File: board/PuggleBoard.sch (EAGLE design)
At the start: 131 parts, among them U1 LMP7704, U10 SN65LVDS2, U11 SN65LVDS1, U12 SN65LVDS1, U13 SN65LVDS1, U14 SN65MLVD201D, U15 24C, U2 ADS8331, U3 OPA4209, U4 AD5686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

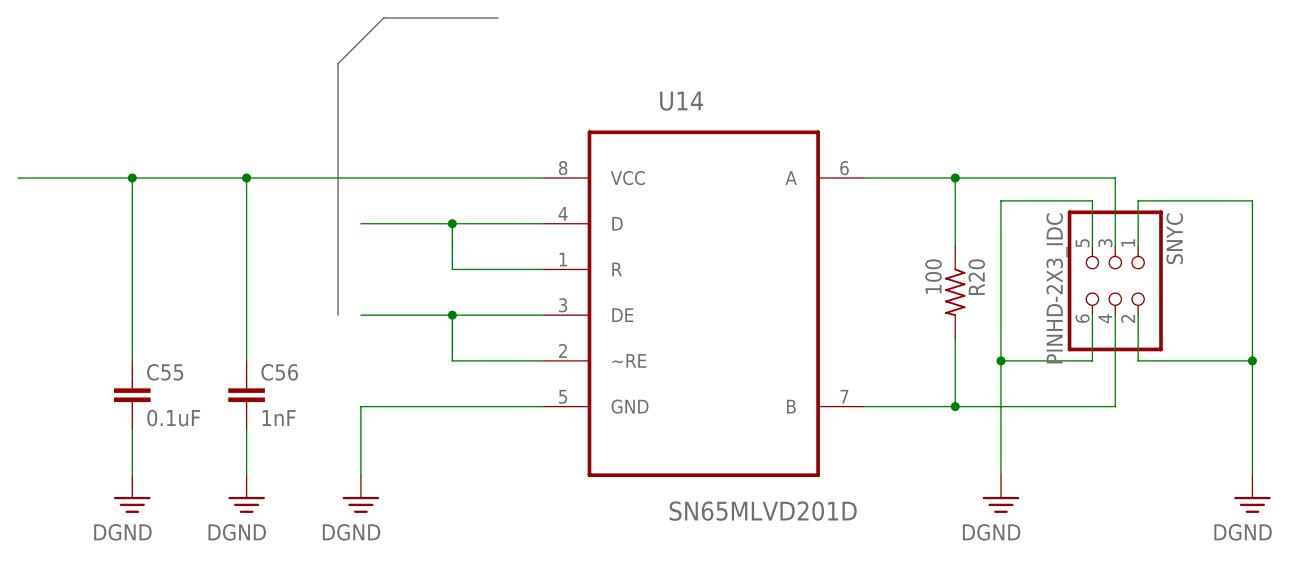
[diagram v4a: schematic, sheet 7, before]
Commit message: Did some of the differential pair wiring.
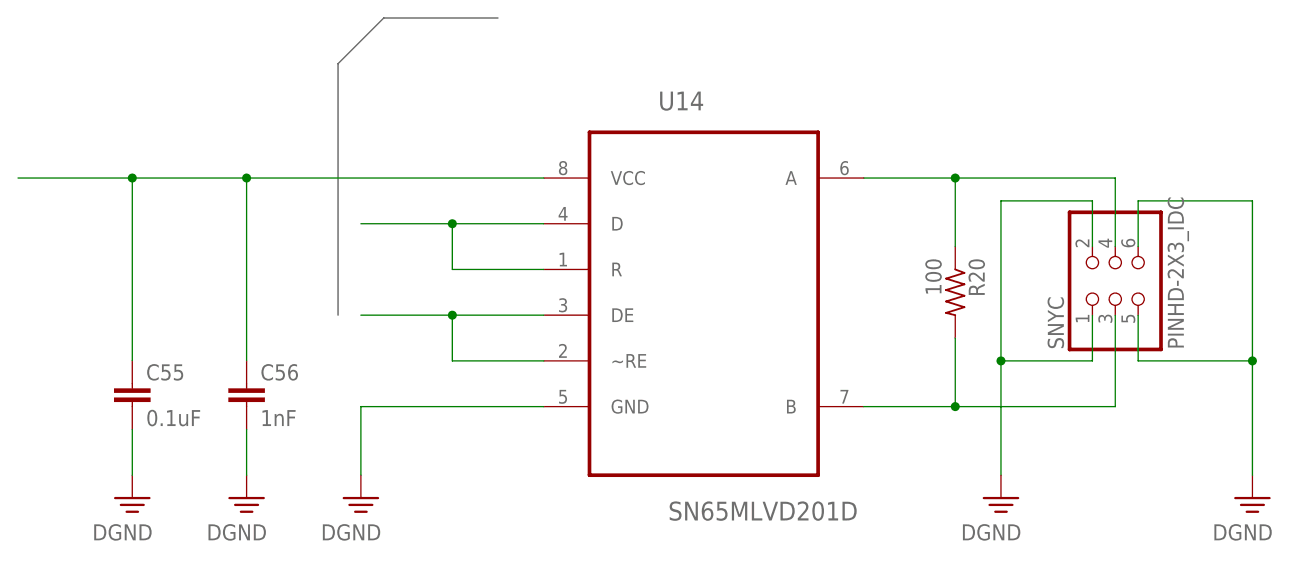
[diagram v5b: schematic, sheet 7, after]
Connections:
- removed net N$11: R20.2, SNYC.4, U14.B
- removed net N$7: R20.1, SNYC.3, U14.A
- new net SYNC_N: R20.2, SNYC.3, U14.B
- new net SYNC_P: R20.1, SNYC.4, U14.A
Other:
- moved on the sheet: SNYC
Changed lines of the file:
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@@
 <instance part="FRAME8" gate="G$2" x="172.72" y="0"/>
 <instance part="U14" gate="A" x="149.86" y="127"/>
-<instance part="SNYC" gate="G$1" x="195.58" y="121.92" rot="R270"/>
+<instance part="SNYC" gate="G$1" x="195.58" y="124.46" rot="R90"/>
 <instance part="R20" gate="R" x="177.8" y="121.92" rot="R270"/>
 <instance part="DGND12" gate="DGND" x="210.82" y="99.06"/>
@@
 </busses>
 <nets>
-<net name="N$11" class="0">
+<net name="SYNC_N" class="2">
 <segment>
 <pinref part="U14" gate="A" pin="B"/>
@@
 <pinref part="R20" gate="R" pin="2"/>
 <wire x1="177.8" y1="109.22" x2="177.8" y2="116.84" width="0.1524" layer="91"/>
-<pinref part="SNYC" gate="G$1" pin="4"/>
 <wire x1="177.8" y1="109.22" x2="195.58" y2="109.22" width="0.1524" layer="91"/>
+<junction x="177.8" y="109.22"/>
+<pinref part="SNYC" gate="G$1" pin="3"/>
 <wire x1="195.58" y1="109.22" x2="195.58" y2="119.38" width="0.1524" layer="91"/>
-<junction x="177.8" y="109.22"/>
 </segment>
 </net>
-<net name="N$7" class="0">
+<net name="SYNC_P" class="2">
 <segment>
 <pinref part="U14" gate="A" pin="A"/>
@@
 <pinref part="R20" gate="R" pin="1"/>
 <wire x1="177.8" y1="127" x2="177.8" y2="134.62" width="0.1524" layer="91"/>
-<pinref part="SNYC" gate="G$1" pin="3"/>
 <wire x1="177.8" y1="134.62" x2="195.58" y2="134.62" width="0.1524" layer="91"/>
+<junction x="177.8" y="134.62"/>
+<pinref part="SNYC" gate="G$1" pin="4"/>
 <wire x1="195.58" y1="134.62" x2="195.58" y2="127" width="0.1524" layer="91"/>
-<junction x="177.8" y="134.62"/>
 </segment>
 </net>
 <net name="GND" class="0">
 <segment>
-<pinref part="SNYC" gate="G$1" pin="1"/>
-<wire x1="198.12" y1="127" x2="198.12" y2="132.08" width="0.1524" layer="91"/>
 <wire x1="198.12" y1="132.08" x2="210.82" y2="132.08" width="0.1524" layer="91"/>
 <wire x1="210.82" y1="132.08" x2="210.82" y2="114.3" width="0.1524" layer="91"/>
-<pinref part="SNYC" gate="G$1" pin="2"/>
-<wire x1="198.12" y1="119.38" x2="198.12" y2="114.3" width="0.1524" layer="91"/>
 <wire x1="198.12" y1="114.3" x2="210.82" y2="114.3" width="0.1524" layer="91"/>
 <wire x1="210.82" y1="114.3" x2="210.82" y2="101.6" width="0.1524" layer="91"/>
 <junction x="210.82" y="114.3"/>
 <pinref part="DGND12" gate="DGND" pin="PE"/>
+<pinref part="SNYC" gate="G$1" pin="5"/>
+<wire x1="198.12" y1="114.3" x2="198.12" y2="119.38" width="0.1524" layer="91"/>
+<pinref part="SNYC" gate="G$1" pin="6"/>
+<wire x1="198.12" y1="132.08" x2="198.12" y2="127" width="0.1524" layer="91"/>
 </segment>
 <segment>
-<pinref part="SNYC" gate="G$1" pin="5"/>
-<wire x1="193.04" y1="127" x2="193.04" y2="132.08" width="0.1524" layer="91"/>
 <wire x1="193.04" y1="132.08" x2="182.88" y2="132.08" width="0.1524" layer="91"/>
 <wire x1="182.88" y1="132.08" x2="182.88" y2="114.3" width="0.1524" layer="91"/>
-<pinref part="SNYC" gate="G$1" pin="6"/>
 <wire x1="182.88" y1="114.3" x2="182.88" y2="101.6" width="0.1524" layer="91"/>
-<wire x1="193.04" y1="119.38" x2="193.04" y2="114.3" width="0.1524" layer="91"/>
 <wire x1="193.04" y1="114.3" x2="182.88" y2="114.3" width="0.1524" layer="91"/>
 <junction x="182.88" y="114.3"/>
 <pinref part="DGND22" gate="DGND" pin="PE"/>
+<pinref part="SNYC" gate="G$1" pin="2"/>
+<wire x1="193.04" y1="132.08" x2="193.04" y2="127" width="0.1524" layer="91"/>
+<pinref part="SNYC" gate="G$1" pin="1"/>
+<wire x1="193.04" y1="114.3" x2="193.04" y2="119.38" width="0.1524" layer="91"/>
 </segment>
 <segment>

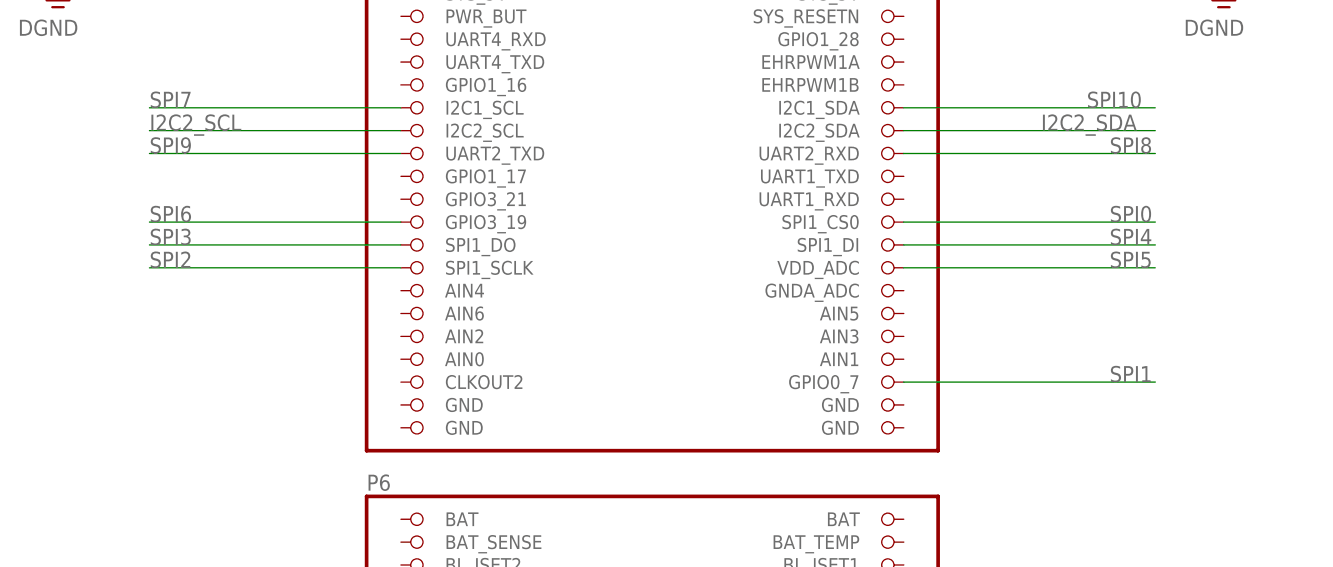
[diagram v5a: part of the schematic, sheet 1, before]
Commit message: updated digital lines with new pinout; EEPROM still using pins 19 and 20
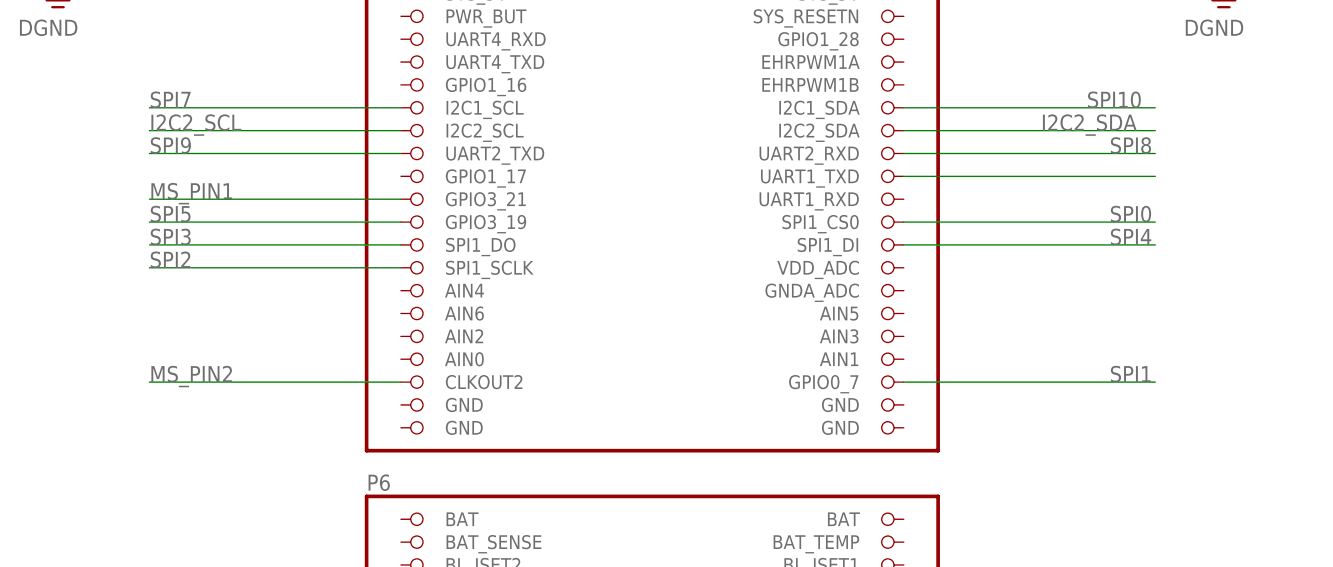
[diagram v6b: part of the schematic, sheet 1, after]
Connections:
- removed net N$12: U14.D, U14.R
- removed net N$17: U14.DE, U14.~RE
- new net MS_PIN1: BB1.GPIO3_21, U14.D, U14.R
- new net MS_PIN2: BB1.CLKOUT2, U14.DE, U14.~RE
- net SPI5: now also BB1.GPIO3_19; no longer BB1.VDD_ADC
- net SPI6: now also BB1.UART1_TXD; no longer BB1.GPIO3_19
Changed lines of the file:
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@@
 <?xml version="1.0" encoding="utf-8"?>
 <!DOCTYPE eagle SYSTEM "eagle.dtd">
-<eagle version="6.5.0">
+<eagle version="6.4">
 <drawing>
 <settings>
@@
 </segment>
 <segment>
-<label x="22.86" y="5.08" size="1.778" layer="95"/>
-<pinref part="BB1" gate="G$1" pin="VDD_ADC"/>
-<wire x1="27.94" y1="5.08" x2="0" y2="5.08" width="0.1524" layer="91"/>
+<pinref part="BB1" gate="G$1" pin="GPIO3_19"/>
+<wire x1="-55.88" y1="10.16" x2="-83.82" y2="10.16" width="0.1524" layer="91"/>
+<label x="-83.82" y="10.16" size="1.778" layer="95"/>
 </segment>
 </net>
@@
 </segment>
 <segment>
-<label x="-83.82" y="10.16" size="1.778" layer="95"/>
-<pinref part="BB1" gate="G$1" pin="GPIO3_19"/>
-<wire x1="-83.82" y1="10.16" x2="-55.88" y2="10.16" width="0.1524" layer="91"/>
+<pinref part="BB1" gate="G$1" pin="UART1_TXD"/>
+<wire x1="0" y1="15.24" x2="27.94" y2="15.24" width="0.1524" layer="91"/>
 </segment>
 </net>
@@
 <pinref part="BB1" gate="G$1" pin="I2C1_SDA"/>
 <wire x1="27.94" y1="22.86" x2="0" y2="22.86" width="0.1524" layer="91"/>
+</segment>
+</net>
+<net name="MS_PIN2" class="0">
+<segment>
+<pinref part="BB1" gate="G$1" pin="CLKOUT2"/>
+<wire x1="-55.88" y1="-7.62" x2="-83.82" y2="-7.62" width="0.1524" layer="91"/>
+<label x="-83.82" y="-7.62" size="1.778" layer="95"/>
+</segment>
+</net>
+<net name="MS_PIN1" class="0">
+<segment>
+<pinref part="BB1" gate="G$1" pin="GPIO3_21"/>
+<wire x1="-55.88" y1="12.7" x2="-83.82" y2="12.7" width="0.1524" layer="91"/>
+<label x="-83.82" y="12.7" size="1.778" layer="95"/>
 </segment>
 </net>
@@
 </segment>
 </net>
-<net name="N$12" class="0">
+<net name="MS_PIN1" class="0">
 <segment>
 <pinref part="U14" gate="A" pin="R"/>
@@
 <junction x="121.92" y="129.54"/>
 <wire x1="121.92" y1="129.54" x2="111.76" y2="129.54" width="0.1524" layer="91"/>
-</segment>
-</net>
-<net name="N$17" class="0">
+<label x="111.76" y="129.54" size="1.778" layer="95"/>
+</segment>
+</net>
+<net name="MS_PIN2" class="0">
 <segment>
 <pinref part="U14" gate="A" pin="~RE"/>
@@
 <junction x="121.92" y="119.38"/>
 <wire x1="121.92" y1="119.38" x2="111.76" y2="119.38" width="0.1524" layer="91"/>
-</segment>
-</net>
+<label x="111.76" y="119.38" size="1.778" layer="95"/>
+</segment>
+</net>

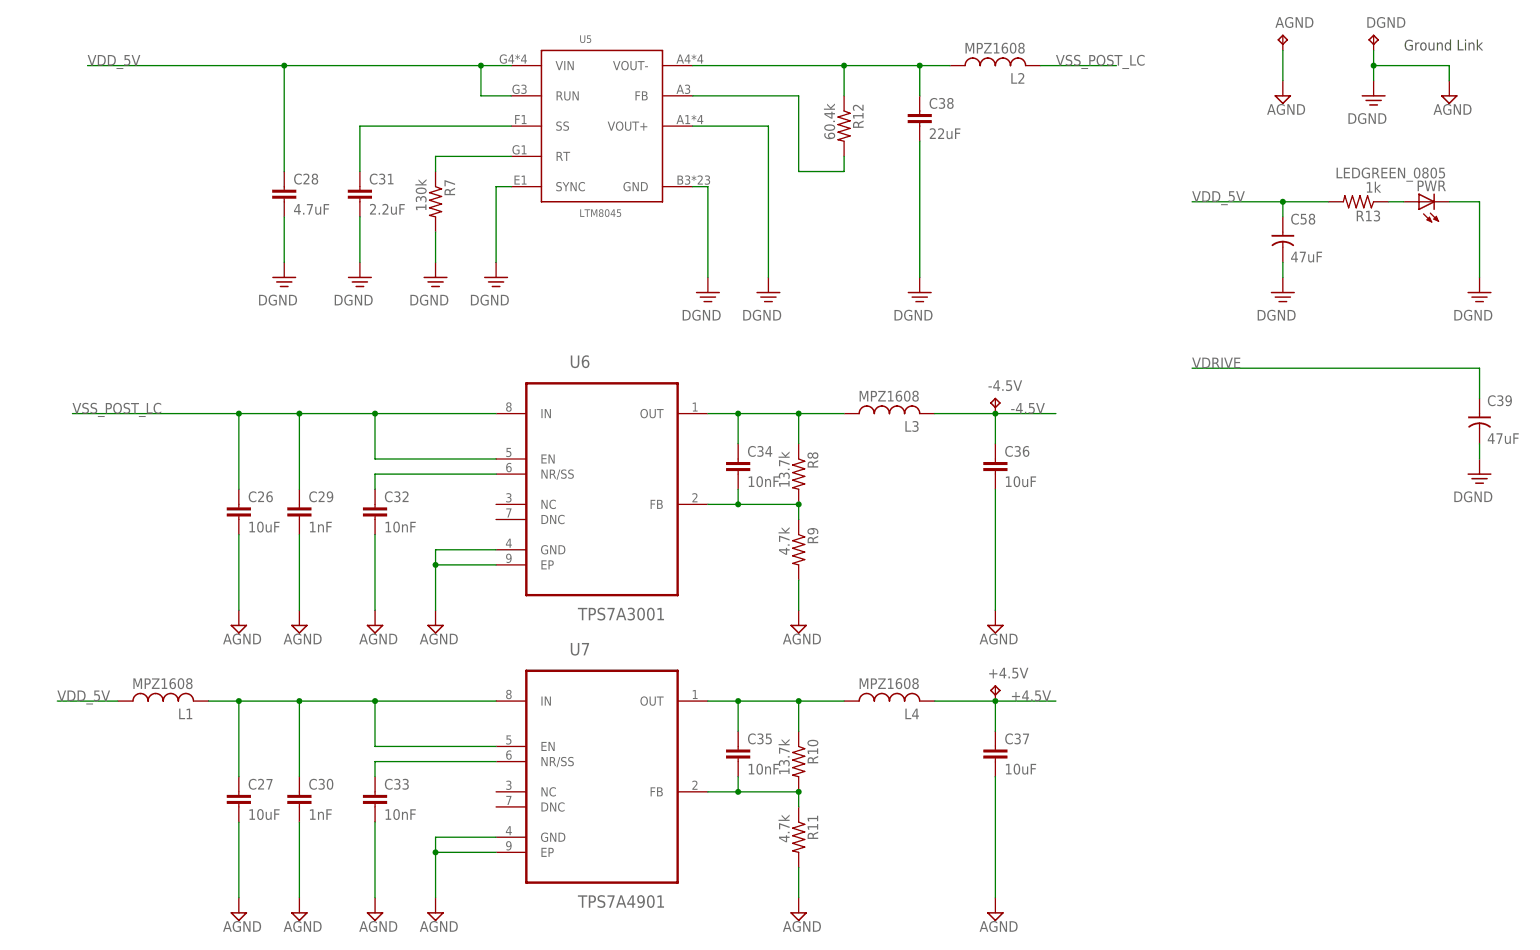
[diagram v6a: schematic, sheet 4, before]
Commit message: Routing complete. Many ERC and DRC fixes.
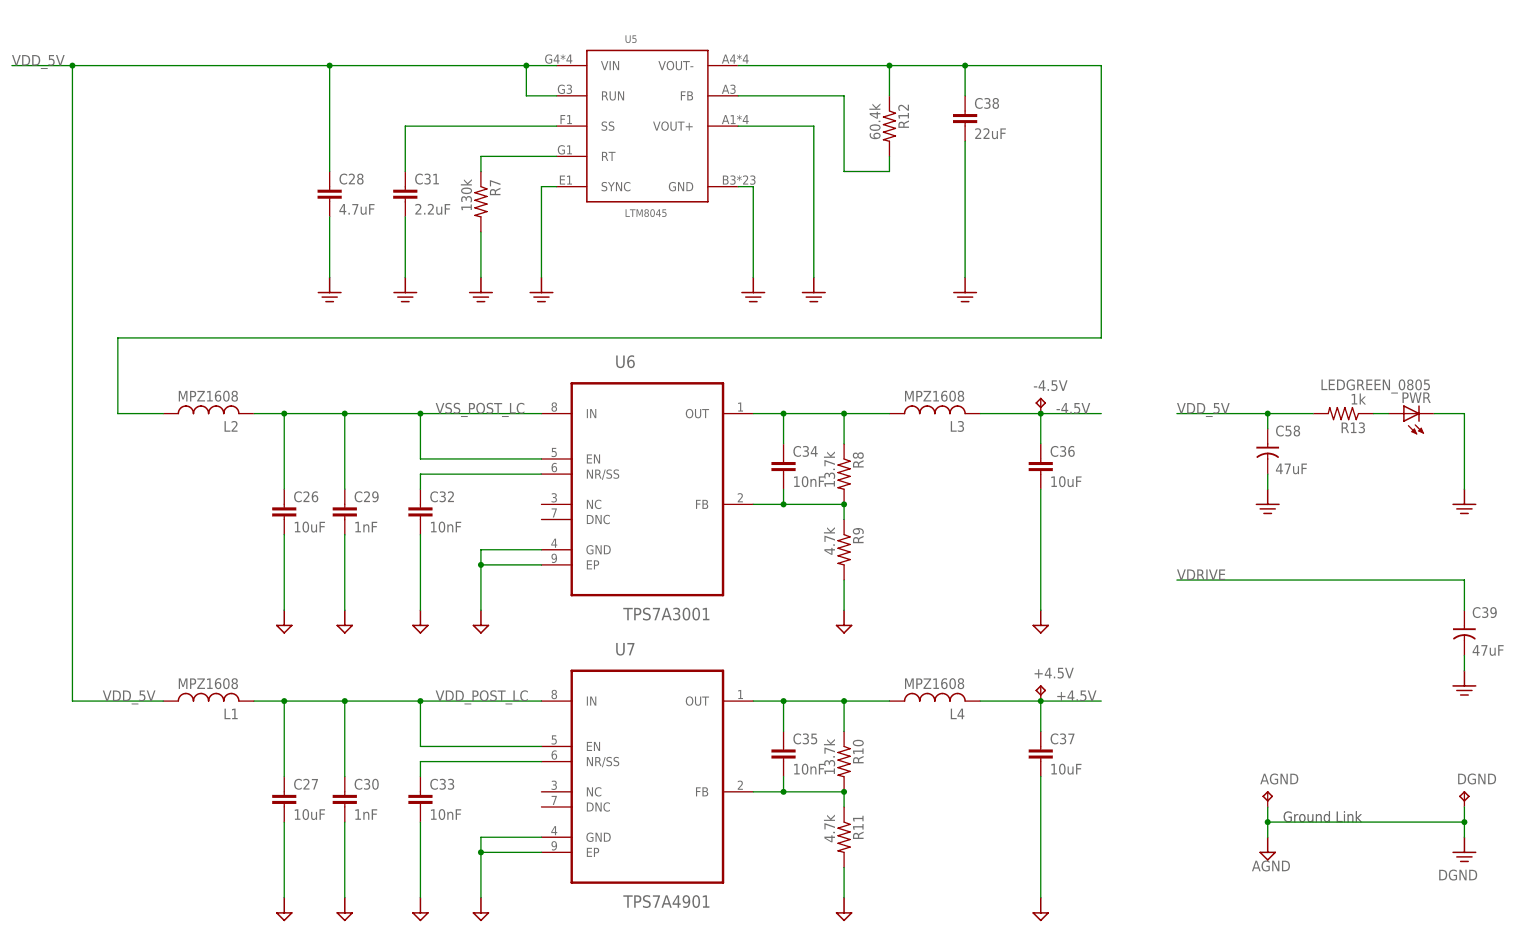
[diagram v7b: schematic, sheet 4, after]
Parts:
- R20: value 100 -> 150
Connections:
- net MS_PIN1 renamed SYNC
- net MS_PIN2 renamed MASTER/SLAVE
- removed net BOARD_TEMP: U8.TEMP
- removed net N$38: U5.SYNC
- net GND: now also BB1.GND@3, BB1.GND@4, BB1.GND@5, BB1.GND@6, U5.SYNC
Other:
- moved on the sheet: +4.5V, -4.5V, AGND, C26, C27, C28, C29, C30, C31, C32, C33, C34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
